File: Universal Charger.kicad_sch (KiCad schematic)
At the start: 35 parts, among them J1 Conn_01x02_Pin, J2 Conn_01x02_Pin, J3 USB_C_Receptacle_USB2.0_16P, J4 Conn_BAT, J5 Conn_01x02_Pin, J6 Conn_01x02_Pin, J7 Conn_01x02_Pin, U6 TP4056, U8 TPS63001, U9 TPS63002

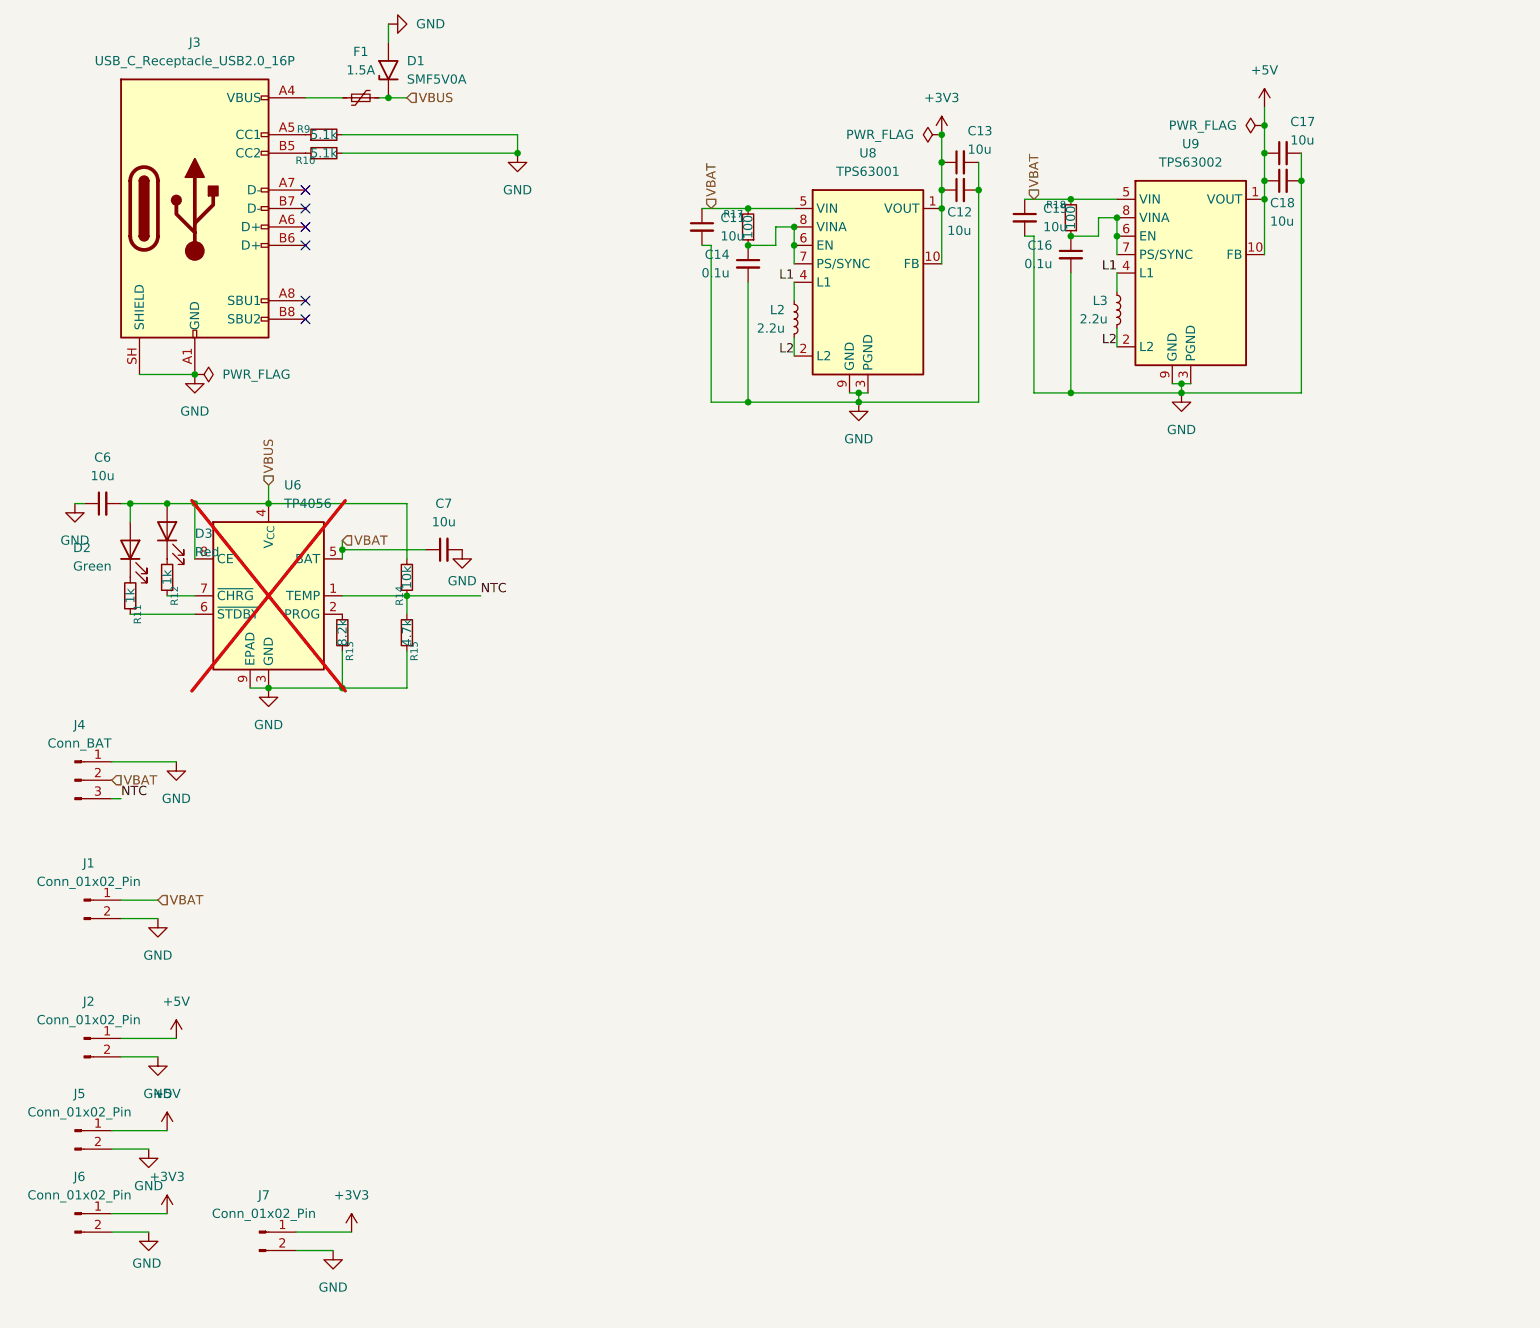
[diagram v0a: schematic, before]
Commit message: Added mounting hole and cleanup
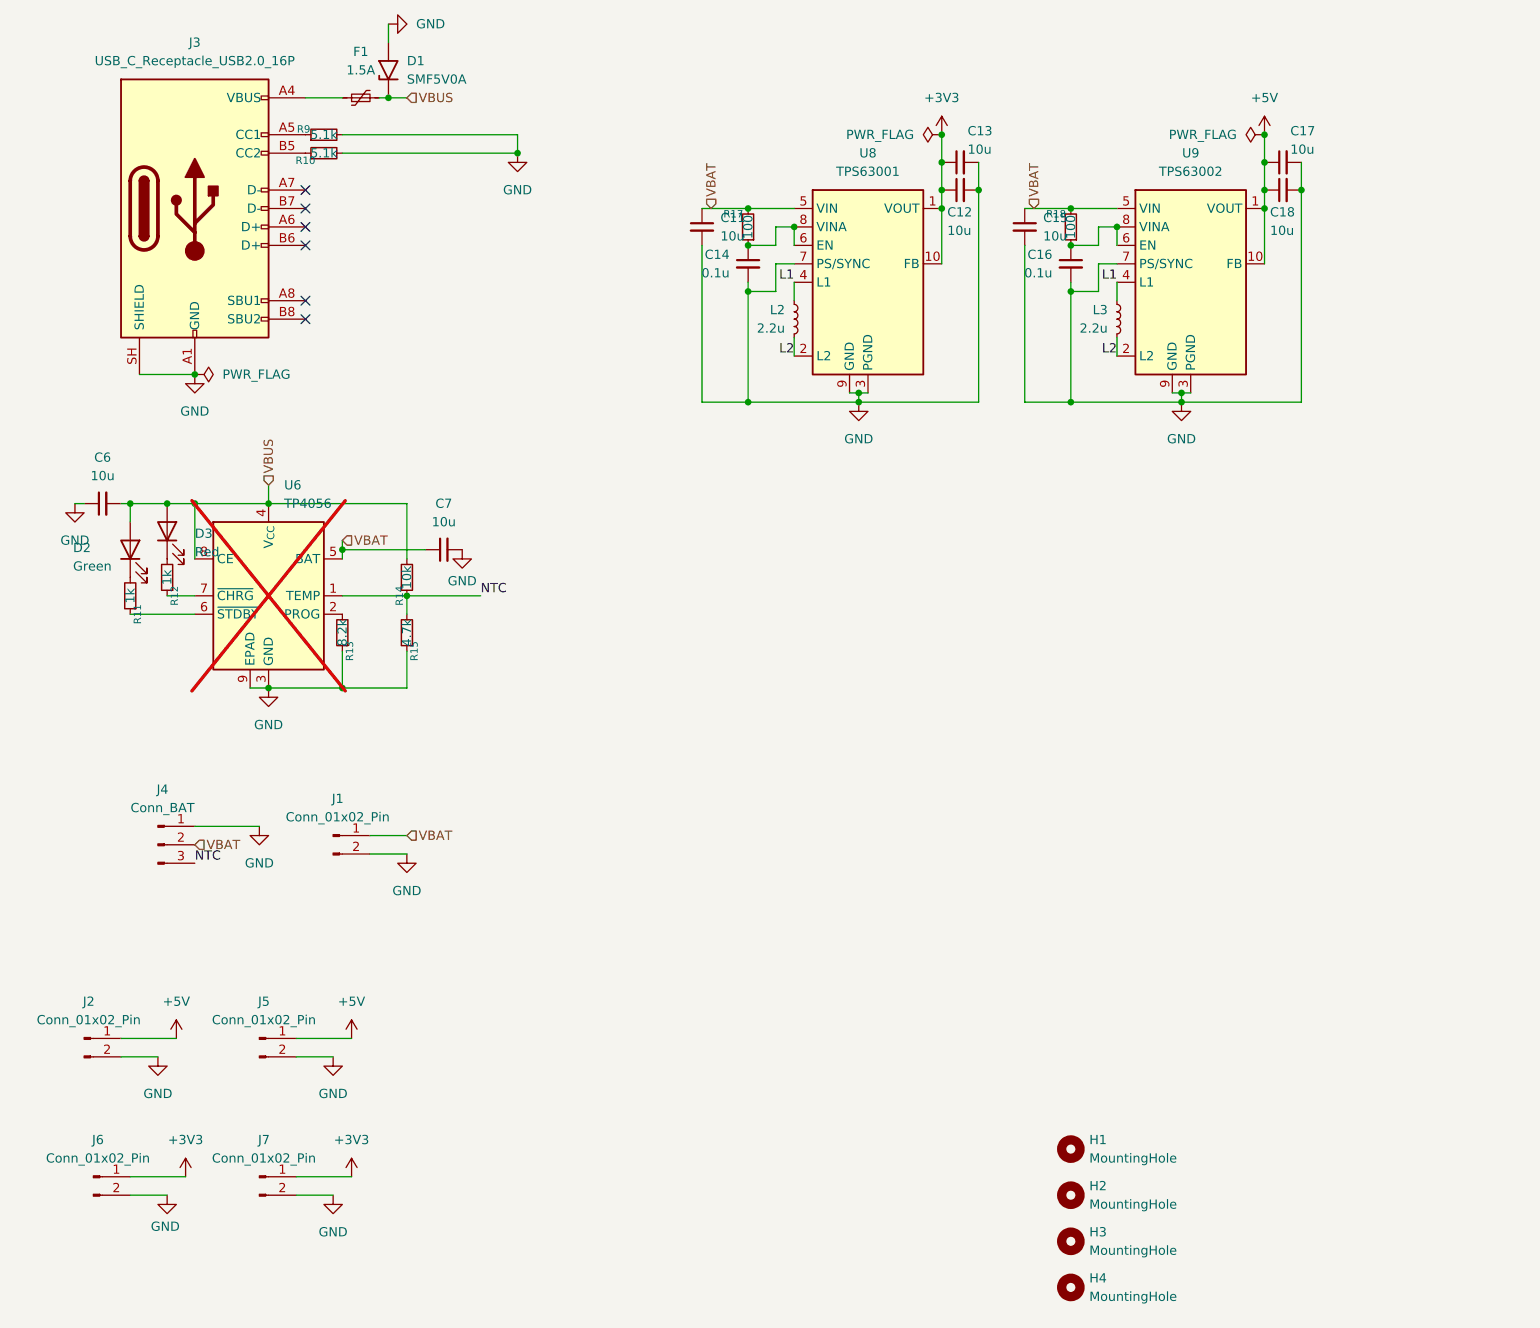
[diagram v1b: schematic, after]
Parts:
- added H1, H2, H3, H4: MountingHole, symbol Mechanical:MountingHole
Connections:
- net GND: now also U8.7 (PS/SYNC), U9.7 (PS/SYNC)
- net at C14.1, R17.1, U8.6 (EN)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: no longer U8.7 (PS/SYNC)
- net at C16.1, R18.1, U9.6 (EN)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: no longer U9.7 (PS/SYNC)
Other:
- moved on the sheet: C15, C16, C17, C18, J1, J4, J5, J6, J7, L3, R18, U9

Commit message: Final PCB Layout
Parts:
- removed C7: 10u, Capacitor_SMD:C_0603_1608Metric, symbol Device:C_Small
- removed R14: 10k, Resistor_SMD:R_0402_1005Metric, symbol Device:R_Small
- removed R15: 4.7k, Resistor_SMD:R_0402_1005Metric, symbol Device:R_Small
- added C10: 10u, Capacitor_SMD:C_0805_2012Metric, symbol Device:C_Small
- added R24: 6.2k, Resistor_SMD:R_0201_0603Metric, symbol Device:R_Small
- C14, C16: footprint Capacitor_SMD:C_0402_1005Metric -> Capacitor_SMD:C_0603_1608Metric
- C6: footprint Capacitor_SMD:C_0603_1608Metric -> Capacitor_SMD:C_0805_2012Metric
- H1, H2, H3, H4: footprint (none) -> MountingHole:MountingHole_2.7mm_M2.5
- J1, J2: footprint (none) -> Connector_PinHeader_2.54mm:PinHeader_1x02_P2.54mm_Vertical
- J4: footprint Connector_JST:JST_PH_B3B-PH-K_1x03_P2.00mm_Vertical -> Connector_PinHeader_1.27mm:PinHeader_1x03_P1.27mm_Vertical
- J5, J6, J7: footprint (none) -> Connector_PinHeader_1.27mm:PinHeader_1x02_P1.27mm_Vertical
- L2, L3: footprint Inductor_SMD:L_APV_ANR3015 -> Inductor_SMD:L_1210_3225Metric
- R10, R11, R12, R17, R18, R9: footprint Resistor_SMD:R_0402_1005Metric -> Resistor_SMD:R_0201_0603Metric
- R13: value 8.2k -> 10k; footprint Resistor_SMD:R_0402_1005Metric -> Resistor_SMD:R_0201_0603Metric
- U6: now fitted; now in the parts list
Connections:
- net GND: now also C10.2
- net NTC: now also R24.1
- net VBAT: now also C10.1
- net VBUS: now also R24.2
- net L1: no longer names the net of L2.2, U8.4 (L1)
- net L1: no longer L3.2, U9.4 (L1)
- net L2: no longer names the net of L2.1, U8.2 (L2)
- net L2: no longer L3.1, U9.2 (L2)
- new net: L3.1, U9.2 (L2)
- new net: L3.2, U9.4 (L1)
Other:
- moved on the sheet: D1, F1, J3, R10, R9

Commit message: Implemented the Universak charger fully including Gerber
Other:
- note added: "29/10/2026"
- note added: "Yashavanta 1MS25EC164"
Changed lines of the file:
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@@
 	(generator_version "10.0")
 	(paper "A4")
+	(text "Yashavanta\n1MS25EC164"
+		(exclude_from_sim no)
+		(at 185.42 170.18 0)
+		(effects
+			(font
+				(size 1.27 1.27)
+			)
+		)
+	)
+	(text "29/10/2026"
+		(exclude_from_sim no)
+		(at 213.36 193.04 0)
+		(effects
+			(font
+				(size 1.27 1.27)
+			)
+		)
+	)
 	(junction
 		(at 184.15 31.75)
@@
 	(wire
 		(pts
-			(xy 36.83 129.54) (xy 41.91 129.54)
+			(xy 36.83 129.54) (xy 39.37 129.54)
 		)
 		(stroke
@@
 	)
 	(label "VBAT"
-		(at 41.91 129.54 0)
+		(at 39.37 129.54 0)
 		(effects
 			(font
@@
 		)
 		(property "Value" "GND"
-			(at 128.27 69.85 0)
+			(at 128.27 72.39 0)
 			(show_name no)
 			(do_not_autoplace no)
